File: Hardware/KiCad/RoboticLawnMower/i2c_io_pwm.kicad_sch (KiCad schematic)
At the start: 9 parts, among them U4 PCA9685PW

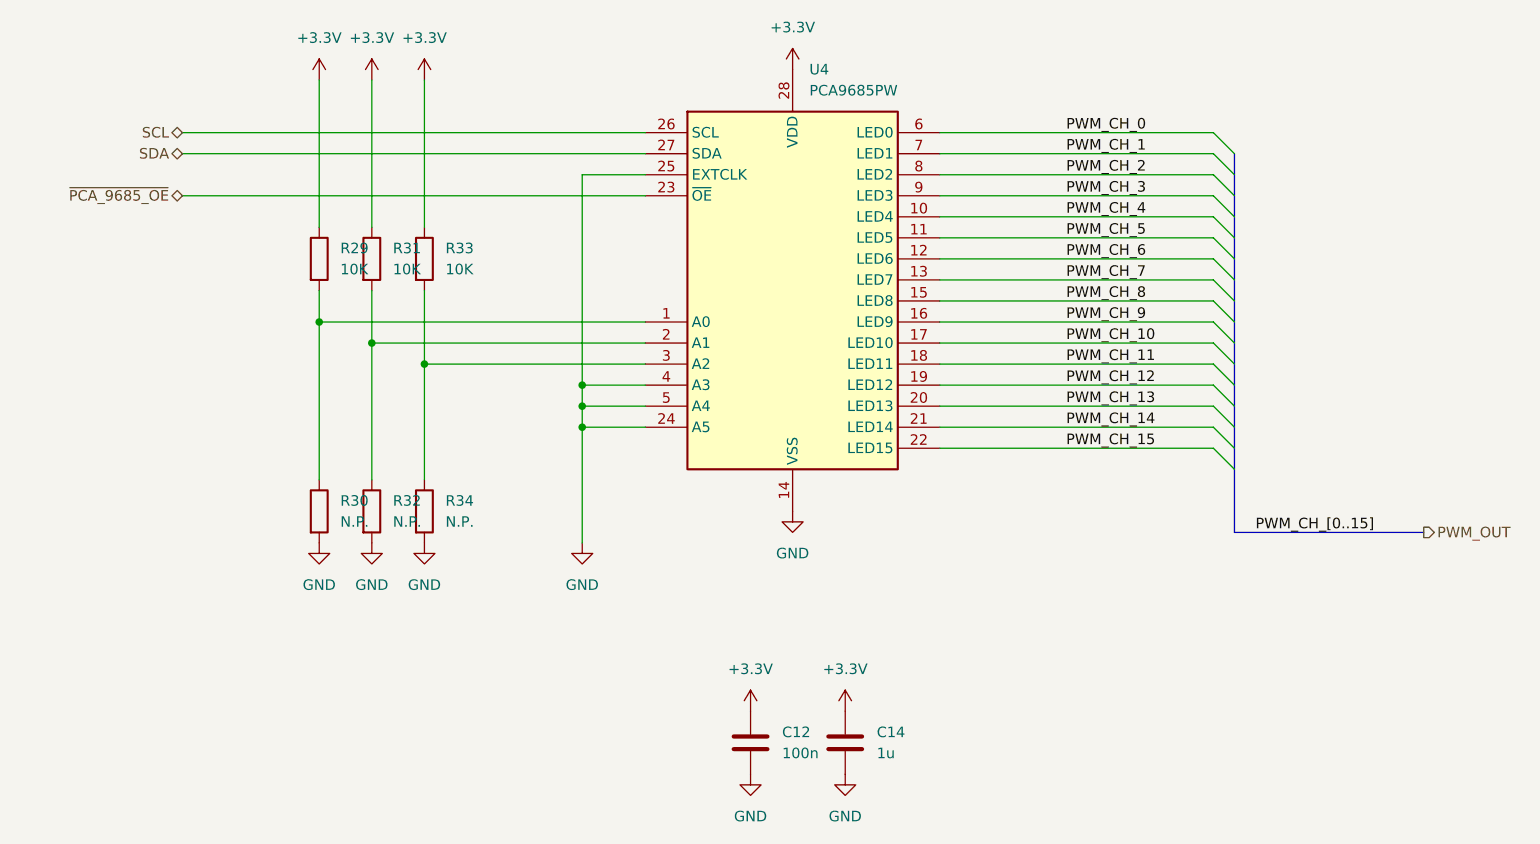
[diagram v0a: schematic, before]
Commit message: Redesign: - Controller - I2C pinning geändert - uvm
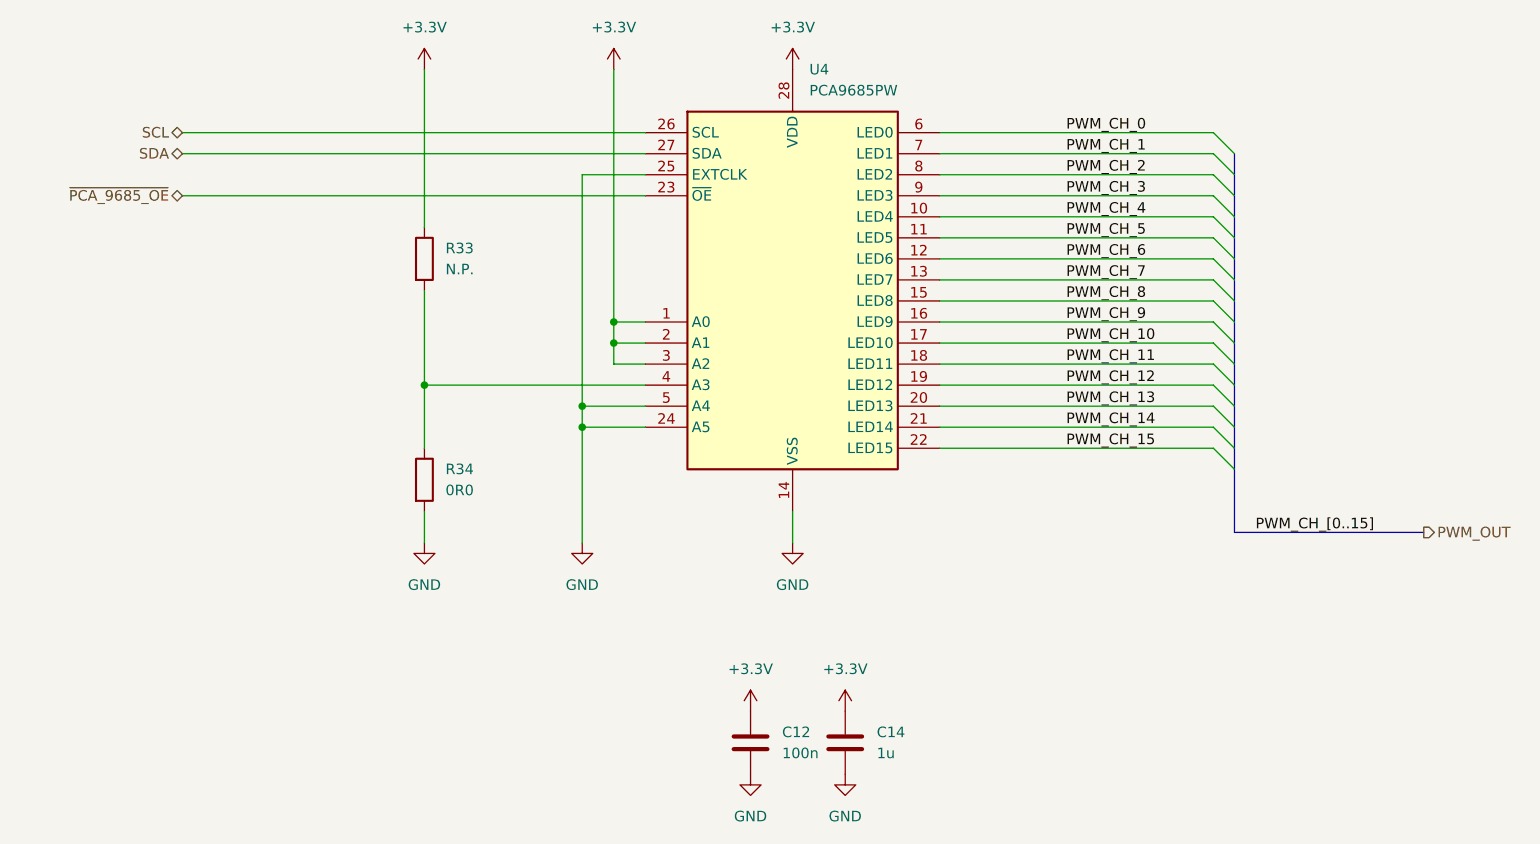
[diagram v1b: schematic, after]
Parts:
- removed R29, R31: 10K, Resistor_SMD:R_0402_1005Metric, symbol Device:R
- removed R30, R32: N.P., Resistor_SMD:R_0402_1005Metric, symbol Device:R
- R33: value 10K -> N.P.
- R34: value N.P. -> 0R0
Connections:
- net +3.3V: now also U4.1 (A0), U4.2 (A1), U4.3 (A2)
- net GND: no longer U4.4 (A3)
- net at R33.2, R34.1: now also U4.4 (A3); no longer U4.3 (A2)
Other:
- moved on the sheet: R34
